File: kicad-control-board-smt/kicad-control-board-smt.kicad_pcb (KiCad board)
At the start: 2 copper layers, 100 x 110 mm, 97 parts, among them J101 Conn_01x10_Female, J102 Conn_01x16_Male, J103 BA56_3DIG_7SEG, J104 Gate Out, J105 Clock Out, J106 Clock In, J107 Pitch Out, J108 CV Out, J109 Reset In, Q101 MMBT3906, Q102 MMBT3906, Q103 MMBT3906, Q104 MMBT3904, Q105 MMBT3904, SW101 Shift, SW102 Play, SW103 Load, SW104 Save, SW105 Repeat, SW106 Mutate, SW107 Glide, SW108 SW_Push, SW109 SW_Push, SW110 SW_Push, SW111 SW_Push, SW112 SW_Push, SW113 SW_Push, SW114 SW_Push, SW115 SW_Push, SW116 Rotary_Encoder, SW117 SW_Push, SW118 SW_Push, SW119 SW_Push, SW120 SW_Push, SW121 SW_Push, SW122 SW_Push, SW123 SW_Push, SW124 SW_Push, U101 74HC595, U102 MCP23S17, U103 74HC595

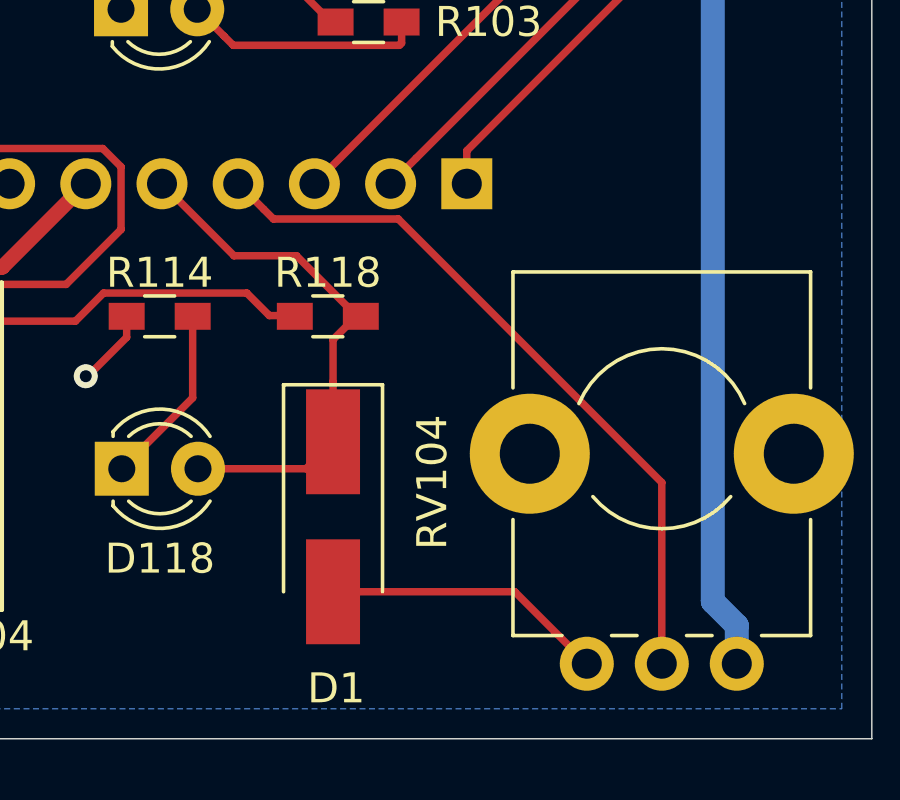
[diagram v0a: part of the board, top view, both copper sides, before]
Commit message: Rerouting traces to avoid potentiometer support lugs shorting to ground
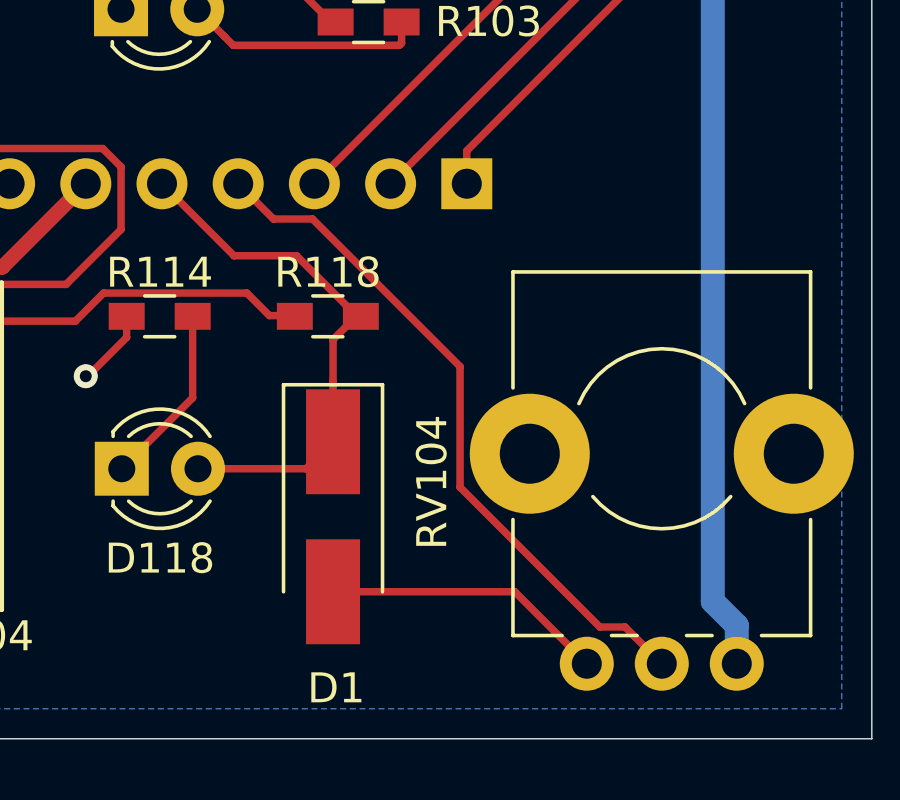
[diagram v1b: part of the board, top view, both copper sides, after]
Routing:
- net AD4: track 24.3 -> 23.1 mm
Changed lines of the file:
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@@
     (thickness 1.6)
     (drawings 11)
-    (tracks 1074)
+    (tracks 1077)
     (zones 0)
     (modules 97)
@@
   (segment (start 75.842096 106.279988) (end 74.042084 108.08) (width 0.5) (layer F.Cu) (net 31))
   (segment (start 85.8 103.5) (end 83.020012 106.279988) (width 0.5) (layer F.Cu) (net 31))
-  (segment (start 91.729999 104.349999) (end 90.88 103.5) (width 0.25) (layer F.Cu) (net 32))
-  (segment (start 92.055001 104.675001) (end 91.729999 104.349999) (width 0.25) (layer F.Cu) (net 32))
-  (segment (start 96.216003 104.675001) (end 92.055001 104.675001) (width 0.25) (layer F.Cu) (net 32))
-  (segment (start 105 113.458998) (end 96.216003 104.675001) (width 0.25) (layer F.Cu) (net 32))
-  (segment (start 105 119.5) (end 105 113.458998) (width 0.25) (layer F.Cu) (net 32))
+  (segment (start 104.100001 118.600001) (end 105 119.5) (width 0.25) (layer F.Cu) (net 32))
+  (segment (start 98.274999 113.616001) (end 102.933997 118.274999) (width 0.25) (layer F.Cu) (net 32))
+  (segment (start 103.774999 118.274999) (end 104.100001 118.600001) (width 0.25) (layer F.Cu) (net 32))
+  (segment (start 98.274999 109.591277) (end 98.274999 113.616001) (width 0.25) (layer F.Cu) (net 32))
+  (segment (start 102.933997 118.274999) (end 103.774999 118.274999) (width 0.25) (layer F.Cu) (net 32))
+  (segment (start 93.358723 104.675001) (end 98.274999 109.591277) (width 0.25) (layer F.Cu) (net 32))
+  (segment (start 92.055001 104.675001) (end 93.358723 104.675001) (width 0.25) (layer F.Cu) (net 32))
+  (segment (start 90.88 103.5) (end 92.055001 104.675001) (width 0.25) (layer F.Cu) (net 32))
   (segment (start 105 91.92) (end 93.42 103.5) (width 0.25) (layer F.Cu) (net 33))
   (segment (start 105 88.75) (end 105 91.92) (width 0.25) (layer F.Cu) (net 33))

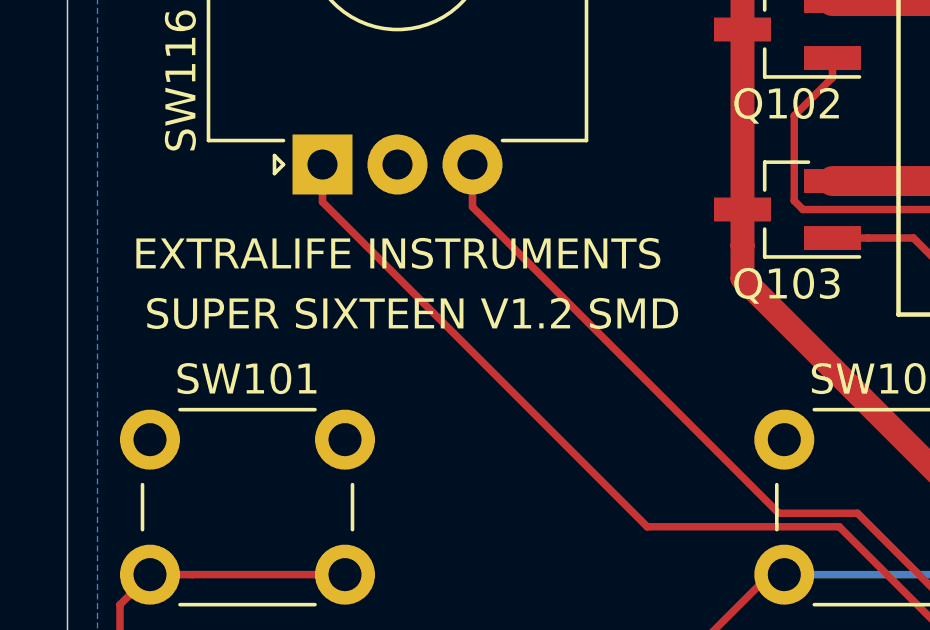
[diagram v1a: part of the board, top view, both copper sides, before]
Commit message: Adding part numbers
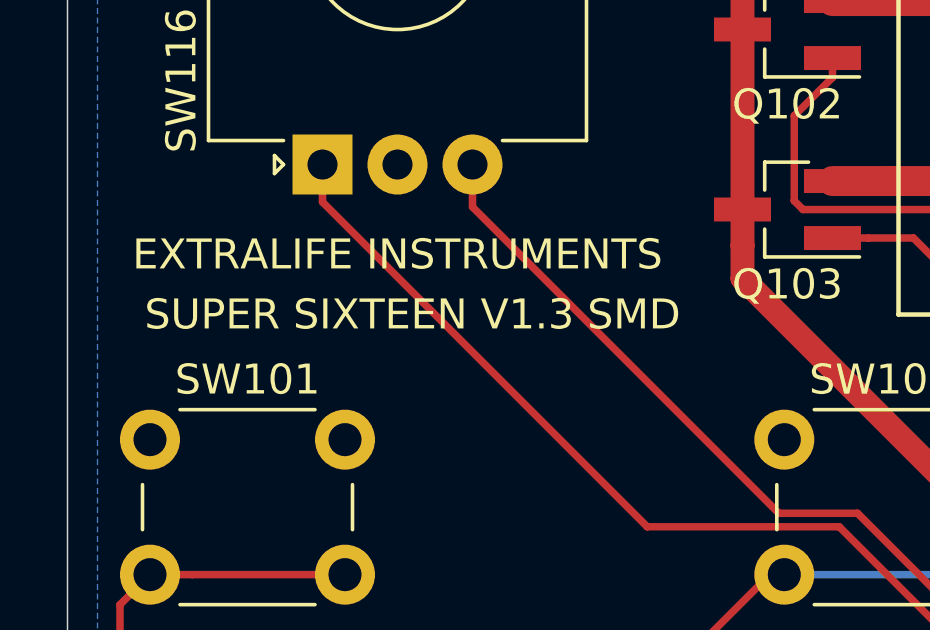
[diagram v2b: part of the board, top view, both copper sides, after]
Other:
- board text added: "SUPER SIXTEEN V1.3 SMD"
- board text removed: "SUPER SIXTEEN V1.2 SMD"
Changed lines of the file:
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@@
     (arrow2b (pts (xy 12 8.5) (xy 13.126504 7.913579)))
   )
-  (gr_text "SUPER SIXTEEN V1.2 SMD" (at 23.5 32.5) (layer F.SilkS)
+  (gr_text "SUPER SIXTEEN V1.3 SMD" (at 23.5 32.5) (layer F.SilkS)
     (effects (font (size 1 1) (thickness 0.15)))
   )

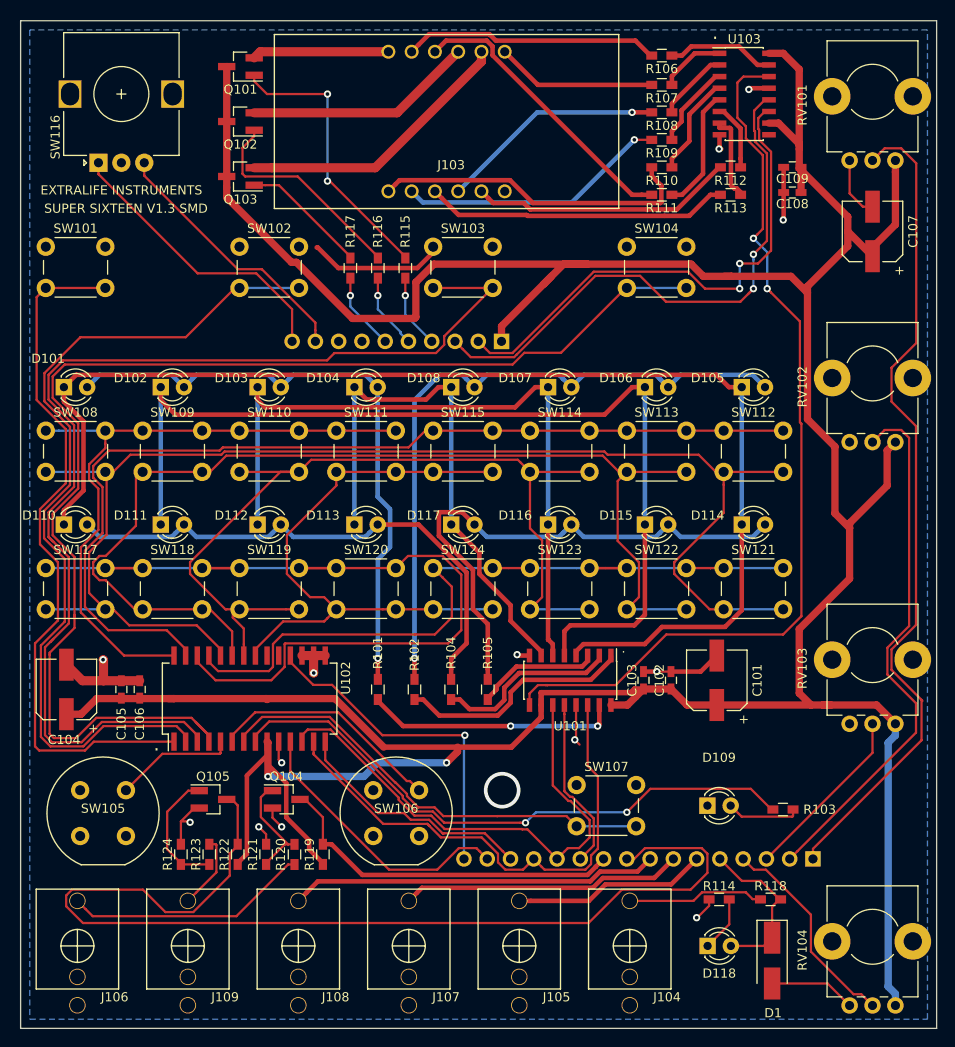
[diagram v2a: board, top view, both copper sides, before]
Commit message: Updating control positions on SMT version
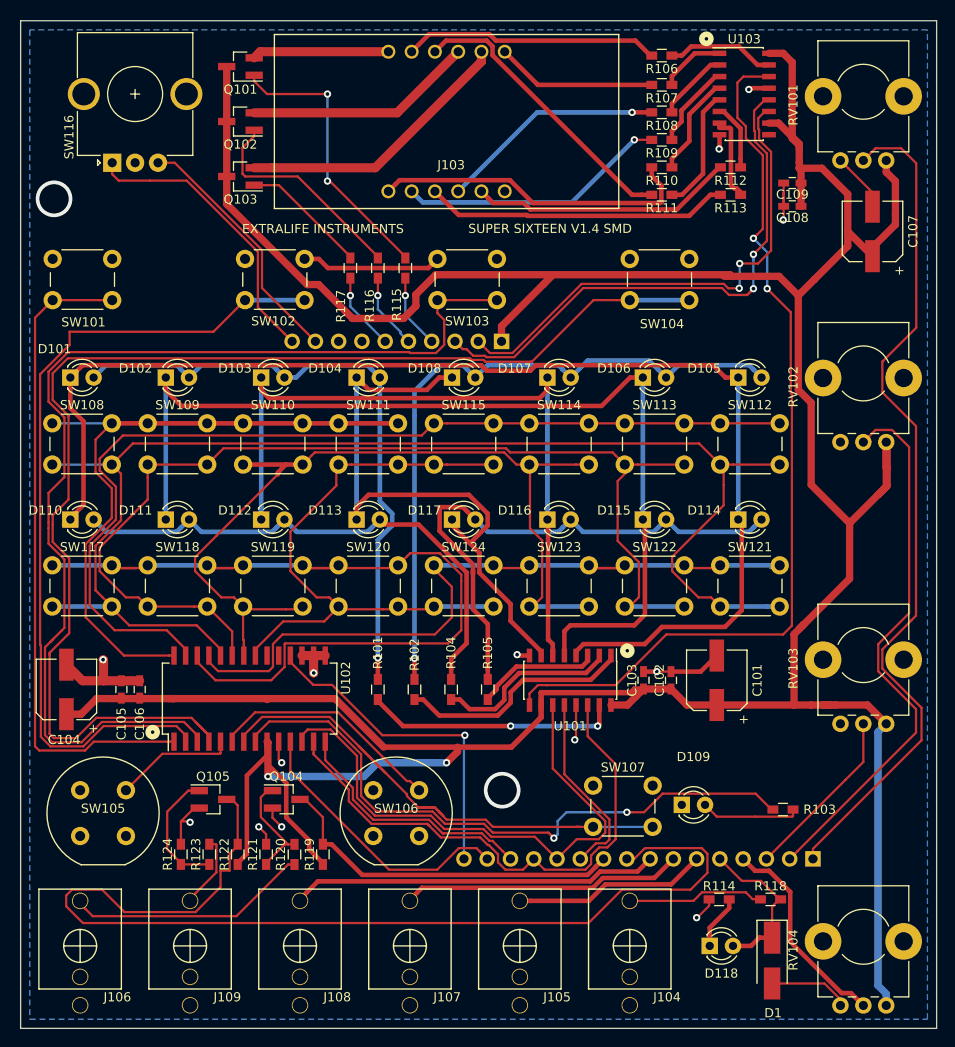
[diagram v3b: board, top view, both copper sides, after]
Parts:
- added G***: LOGO, Super Sixteen Logos:extralife_instruments_logo_medium, B.Cu at (53.1, 112.3)
- added REF***: OSHW-Logo2_7.3x6mm_SilkScreen, Symbols:OSHW-Logo2_7.3x6mm_SilkScreen, B.Cu at (39.1, 21.8)
- added REF***: WEEE-Logo_5.6x8mm_SilkScreen, Symbols:WEEE-Logo_5.6x8mm_SilkScreen, B.Cu at (51.1, 22.4)
- added REF***: RoHS-Logo_6mm_SilkScreen, Symbols:RoHS-Logo_6mm_SilkScreen, B.Cu at (83.3, 21.8)
- added REF***: CE-Logo_8.5x6mm_SilkScreen, Symbols:CE-Logo_8.5x6mm_SilkScreen, B.Cu at (63.8, 21.8)
- moved D109 2.80 mm to (84.2, 97.6)
- moved SW107 1.80 mm to (74.5, 95.5)
- moved C109 1.72 mm to (96.2, 29.7)
- moved SW101 1.53 mm to (15.5, 38.0)
- moved C108 1.51 mm to (96.2, 32.3)
- moved SW116 1.50 mm to (22.0, 27.5)
- moved SW102 1.46 mm to (36.5, 38.0)
- moved SW103 1.41 mm to (57.5, 38.0)
- moved SW104 1.37 mm to (78.5, 38.0)
- moved D101 1.26 mm to (17.4, 51.0)
- moved D102 1.19 mm to (27.8, 51.0)
- moved D103 1.12 mm to (38.3, 51.0)
- moved D105 1.12 mm to (90.3, 51.0)
- moved D104 1.08 mm to (48.7, 51.0)
- moved D106 1.07 mm to (79.9, 51.0)
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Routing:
- net /A6: track 49.5 -> 59.6 mm
- net GND: track 95.8 -> 88.3 mm, vias 14 -> 13
- net Net-(D104-Pad1): track 60.1 -> 66.5 mm
- net /A0: track 77.1 -> 71.8 mm
- net /A2: track 123.3 -> 118.4 mm
- net SCK: track 55.6 -> 60.1 mm
- net /A7: track 65.0 -> 69.3 mm
- net /A1: track 94.4 -> 90.9 mm
- net Net-(SW110-Pad2): track 99.7 -> 96.3 mm
- net Net-(SW109-Pad2): track 119.1 -> 116.2 mm
- net MOSI: track 57.1 -> 59.9 mm
- net Net-(D109-Pad2): track 8.04 -> 10.9 mm
- net AD1: track 91.7 -> 94.2 mm
- net Net-(SW111-Pad2): track 65.8 -> 63.6 mm
- net /A3: track 139.7 -> 137.6 mm
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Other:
- board text added: "SUPER SIXTEEN SMD v1.4 © 2020"
- board text added: "SUPER SIXTEEN V1.4 SMD"
- board text removed: "."
- board text removed: "SUPER SIXTEEN V1.3 SMD"

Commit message: Updating SMT control board silkscreen
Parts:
- removed the REF*** at (39.1, 21.8)
- added REF***: OSHW-Logo2_9.8x8mm_Copper, Symbols:OSHW-Logo2_9.8x8mm_Copper, B.Cu at (24.3, 21.0)
- moved REF*** 8.50 mm to (42.7, 21.0)
- moved REF*** 5.95 mm to (57.9, 20.7)
- moved REF*** 3.02 mm to (80.5, 20.7)

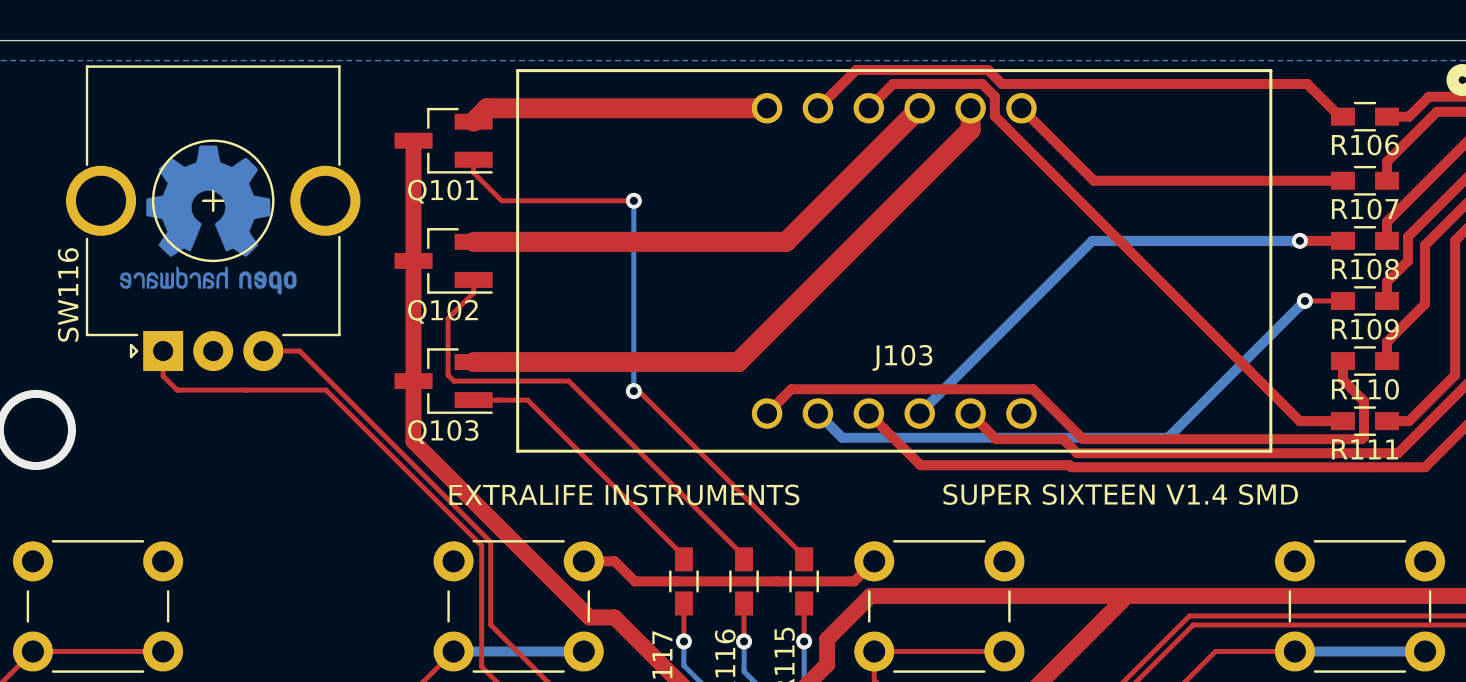
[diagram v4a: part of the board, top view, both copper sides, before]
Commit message: Flipping SMT MMBT2N3906 transistor orientation
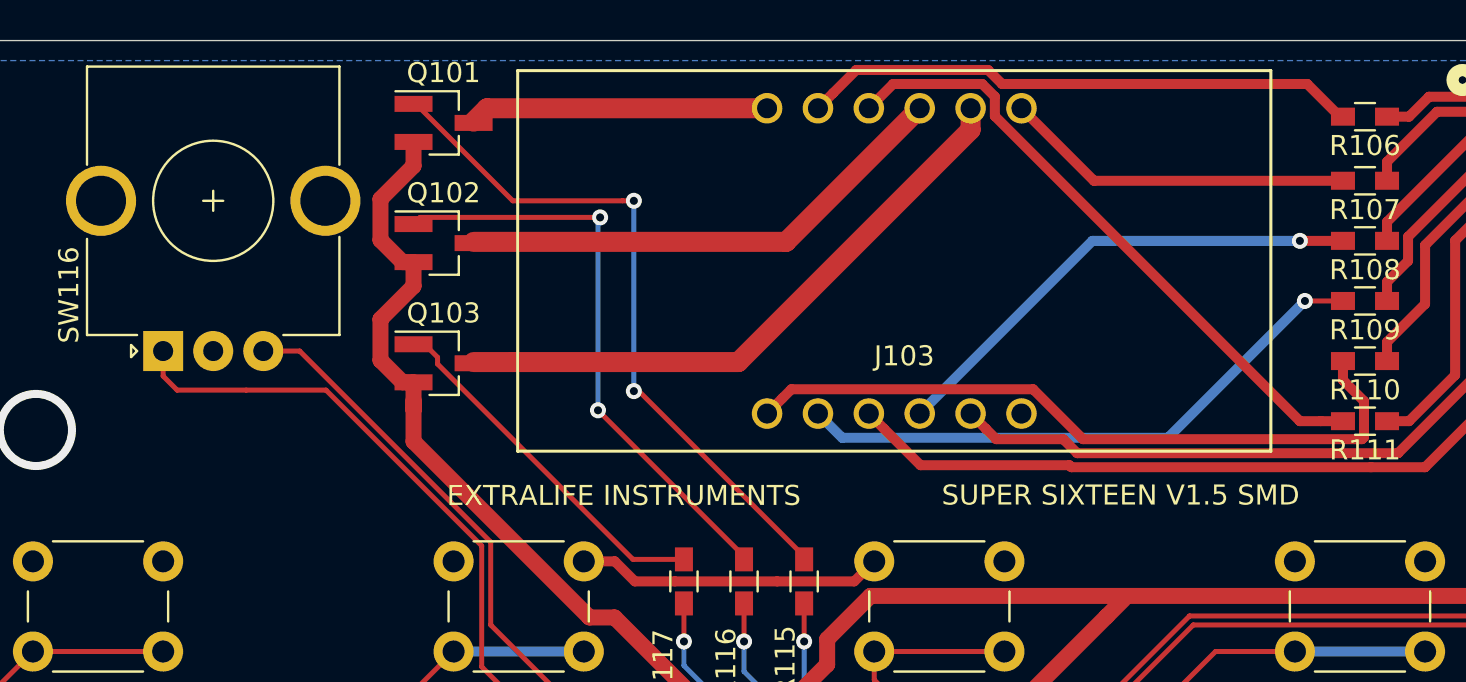
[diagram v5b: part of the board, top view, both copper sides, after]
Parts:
- removed G***: LOGO, Super Sixteen Logos:extralife_instruments_logo_medium
- removed REF***: OSHW-Logo2_9.8x8mm_Copper, Symbols:OSHW-Logo2_9.8x8mm_Copper
- removed REF***: WEEE-Logo_5.6x8mm_SilkScreen, Symbols:WEEE-Logo_5.6x8mm_SilkScreen
- removed REF***: RoHS-Logo_6mm_SilkScreen, Symbols:RoHS-Logo_6mm_SilkScreen
- removed REF***: CE-Logo_8.5x6mm_SilkScreen, Symbols:CE-Logo_8.5x6mm_SilkScreen
- J102: value Conn_01x16_Male -> Conn_01x16_Female
- moved Q101 0.89 mm to (36.0, 16.1), turned to 0 degrees
- moved Q102 0.89 mm to (36.0, 22.1), turned to 0 degrees
- moved Q103 0.89 mm to (36.0, 28.1), turned to 0 degrees
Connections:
- Q101 pad 2: Net-(J103-Pad12) -> +5V
- Q101 pad 3: +5V -> Net-(J103-Pad12)
- Q102 pad 2: Net-(J103-Pad9) -> +5V
- Q102 pad 3: +5V -> Net-(J103-Pad9)
- Q103 pad 2: Net-(J103-Pad8) -> +5V
- Q103 pad 3: +5V -> Net-(J103-Pad8)
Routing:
- net Net-(Q102-Pad1): track 24.0 -> 29.6 mm, vias 0 -> 2
- net Net-(Q103-Pad1): track 13.9 -> 18.1 mm
- net +5V: track 415.6 -> 419.5 mm
- net Net-(Q101-Pad1): track 30.8 -> 34.6 mm
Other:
- board text added: "SUPER SIXTEEN V1.5 SMD"
- board text removed: "SUPER SIXTEEN V1.4 SMD"
